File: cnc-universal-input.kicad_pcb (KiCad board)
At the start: 2 copper layers, 96.5 x 96.5 mm, 161 parts, among them J1 SA, J10 pwr-in, J11 output, J12 USB_B_Mini, J13 ext-pwr, J2 SB, J3 SC, J4 SD, J5 SE, J6 SF, J7 SG, J8 SH, J9 AVR-ISP-6, Q1 2N7002, Q10 IRLML2244TRPBF, Q11 2N7002, Q12 2N7002, Q13 2N7002, Q2 2N7002, Q3 2N7002, Q4 2N7002, Q5 2N7002, Q6 2N7002, Q7 2N7002, Q8 2N7002, Q9 2N7002, SW1 RESET, SW2 BTN, U1 ATmega328PB, U10 SFH617A-4, U11 SFH617A-4, U12 SFH617A-4, U13 SFH617A-4, U14 SFH617A-4, U15 SFH617A-4, U16 SFH617A-4, U17 SFH617A-4, U18 CH340G, U2 74HC595, U3 74HC595, U4 74HC595, U5 4051, U6 L7812, U7 L7805, U8 LM7321, U9 SFH617A-4, Y1 20Mhz, Y2 12MHz

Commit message: Fixed 340G isolation issue
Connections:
- C10 pad 1: VBUS -> +5V
- C21 pad 1: VBUS -> +5V
- J12 pad 1: VBUS -> (no net)
- J12 pad 4: Net-(J12-Pad4) -> (no net)
- R66 pad 1: VBUS -> +5V
- R67 pad 1: VBUS -> +5V
- U18 pad 10: Net-(U18-Pad10) -> (no net)
- U18 pad 11: Net-(U18-Pad11) -> (no net)
- U18 pad 12: Net-(U18-Pad12) -> (no net)
- U18 pad 13: Net-(U18-Pad13) -> (no net)
- U18 pad 14: Net-(U18-Pad14) -> (no net)
- U18 pad 15: Net-(U18-Pad15) -> (no net)
- U18 pad 16: VBUS -> +5V
- U18 pad 9: Net-(U18-Pad9) -> (no net)
- U2 pad 9: Net-(U2-Pad9) -> (no net)
- U3 pad 9: Net-(U3-Pad9) -> (no net)
- U4 pad 9: Net-(U4-Pad9) -> (no net)
- U8 pad 1: Net-(U8-Pad1) -> (no net)
- U8 pad 5: Net-(U8-Pad5) -> (no net)
- U8 pad 8: Net-(U8-Pad8) -> (no net)
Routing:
- net +5V: track 161.7 -> 235.6 mm, vias 4 -> 8
- net VBUS: track 51.0 -> 0.00 mm
- net GND: vias 234 -> 238

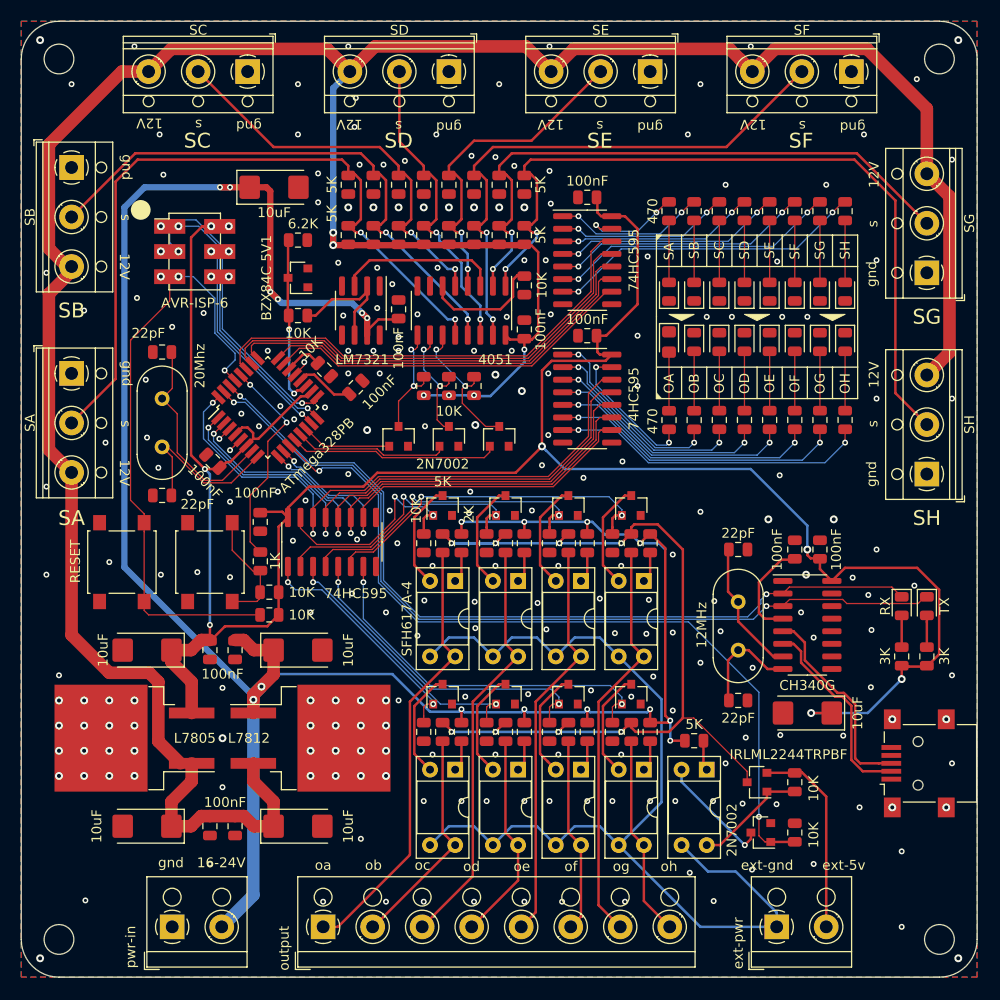
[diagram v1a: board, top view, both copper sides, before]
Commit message: Changed the voltage divider
Forgot to change R2 to 10K/7K so the input voltage to the adc was a bit low. 4.5 instead of 4.9.
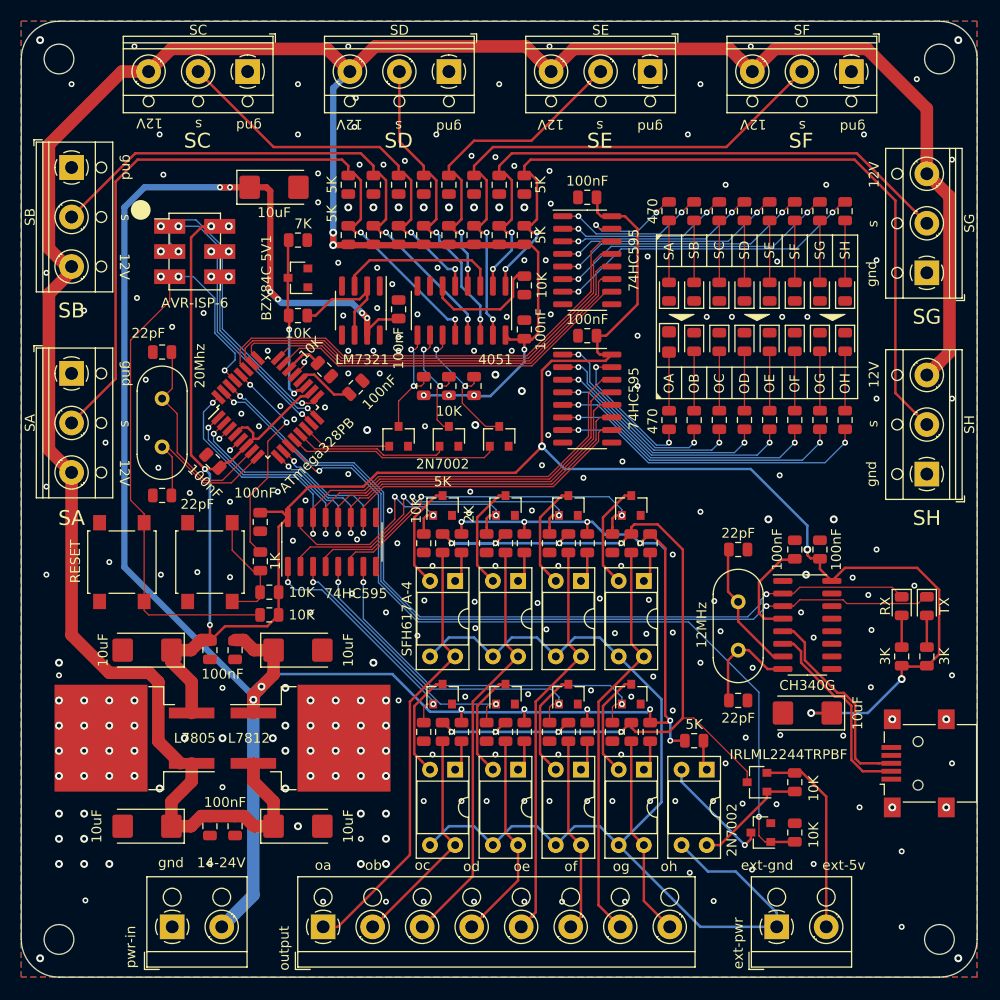
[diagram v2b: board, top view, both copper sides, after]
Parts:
- R35: value 6.2K -> 7K
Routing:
- net GND: vias 238 -> 260
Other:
- board text added: "14-24V"
- board text removed: "16-24V"
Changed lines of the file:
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@@
     (thickness 1.6)
     (drawings 85)
-    (tracks 1603)
+    (tracks 1625)
     (zones 0)
     (modules 161)
@@
       (effects (font (size 1 1) (thickness 0.15)))
     )
-    (fp_text value 6.2K (at 0.508 -1.651 180) (layer F.SilkS)
+    (fp_text value 7K (at 0.508 -1.651 180) (layer F.SilkS)
       (effects (font (size 1 1) (thickness 0.15)))
     )
@@
     (effects (font (size 1 1) (thickness 0.15)))
   )
-  (gr_text 16-24V (at 195.453 -24.257) (layer F.SilkS)
+  (gr_text 14-24V (at 195.453 -24.257) (layer F.SilkS)
     (effects (font (size 1 1) (thickness 0.15)))
   )
@@
   (via (at 250.698 -58.928) (size 0.8) (drill 0.4) (layers F.Cu B.Cu) (net 2))
   (via (at 195.58 -36.83) (size 0.8) (drill 0.4) (layers F.Cu B.Cu) (net 2))
+  (via (at 179.07 -29.21) (size 0.8) (drill 0.4) (layers F.Cu B.Cu) (net 2))
+  (via (at 179.07 -26.67) (size 0.8) (drill 0.4) (layers F.Cu B.Cu) (net 2))
+  (via (at 179.07 -24.13) (size 0.8) (drill 0.4) (layers F.Cu B.Cu) (net 2))
+  (via (at 181.61 -29.21) (size 0.8) (drill 0.4) (layers F.Cu B.Cu) (net 2))
+  (via (at 181.61 -26.67) (size 0.8) (drill 0.4) (layers F.Cu B.Cu) (net 2))
+  (via (at 181.61 -24.13) (size 0.8) (drill 0.4) (layers F.Cu B.Cu) (net 2))
+  (via (at 179.07 -44.45) (size 0.8) (drill 0.4) (layers F.Cu B.Cu) (net 2))
+  (via (at 212.09 -29.21) (size 0.8) (drill 0.4) (layers F.Cu B.Cu) (net 2))
+  (via (at 209.55 -29.21) (size 0.8) (drill 0.4) (layers F.Cu B.Cu) (net 2))
+  (via (at 212.09 -26.67) (size 0.8) (drill 0.4) (layers F.Cu B.Cu) (net 2))
+  (via (at 212.09 -24.13) (size 0.8) (drill 0.4) (layers F.Cu B.Cu) (net 2))
+  (via (at 209.55 -24.13) (size 0.8) (drill 0.4) (layers F.Cu B.Cu) (net 2))
+  (via (at 210.82 -44.45) (size 0.8) (drill 0.4) (layers F.Cu B.Cu) (net 2))
+  (via (at 200.66 -36.83) (size 0.8) (drill 0.4) (layers F.Cu B.Cu) (net 2))
+  (via (at 201.93 -41.91) (size 0.8) (drill 0.4) (layers F.Cu B.Cu) (net 2))
+  (via (at 201.93 -31.75) (size 0.8) (drill 0.4) (layers F.Cu B.Cu) (net 2))
+  (via (at 201.93 -35.56) (size 0.8) (drill 0.4) (layers F.Cu B.Cu) (net 2))
+  (via (at 201.93 -38.1) (size 0.8) (drill 0.4) (layers F.Cu B.Cu) (net 2))
+  (via (at 191.77 -36.83) (size 0.8) (drill 0.4) (layers F.Cu B.Cu) (net 2))
+  (via (at 189.23 -31.75) (size 0.8) (drill 0.4) (layers F.Cu B.Cu) (net 2))
+  (via (at 184.15 -24.13) (size 0.8) (drill 0.4) (layers F.Cu B.Cu) (net 2))
+  (via (at 203.2 -27.94) (size 0.8) (drill 0.4) (layers F.Cu B.Cu) (net 2))
   (segment (start 190.509 -65.215) (end 190.509 -61.341) (width 0.127) (layer F.Cu) (net 3))
   (segment (start 189.484 -66.24) (end 190.509 -65.215) (width 0.127) (layer F.Cu) (net 3))
@@
   (segment (start 254.635 -55.88) (end 254.635 -55.314315) (width 0.25) (layer F.Cu) (net 6))
   (segment (start 254.958315 -54.991) (end 255.52599 -54.991) (width 0.25) (layer F.Cu) (net 6))
+  (segment (start 264.86 -44.06) (end 266.7 -44.06) (width 0.254) (layer F.Cu) (net 6))
+  (segment (start 264.16 -44.06) (end 264.86 -44.06) (width 0.254) (layer F.Cu) (net 6))
+  (segment (start 255.905 -53.91) (end 257.11 -52.705) (width 0.254) (layer F.Cu) (net 6))
+  (segment (start 255.905 -54.855) (end 255.905 -53.91) (width 0.254) (layer F.Cu) (net 6))
+  (segment (start 267.94 -51.81) (end 267.94 -45.3) (width 0.254) (layer F.Cu) (net 6))
+  (segment (start 265.72 -54.03) (end 267.94 -51.81) (width 0.254) (layer F.Cu) (net 6))
+  (segment (start 267.94 -45.3) (end 266.7 -44.06) (width 0.254) (layer F.Cu) (net 6))
+  (segment (start 257.11 -52.705) (end 258.435 -54.03) (width 0.254) (layer F.Cu) (net 6))
+  (segment (start 258.435 -54.03) (end 265.72 -54.03) (width 0.254) (layer F.Cu) (net 6))
+  (via (at 255.016 -39.37) (size 0.8) (drill 0.4) (layers F.Cu B.Cu) (net 6))
+  (segment (start 257.0975 -39.37) (end 255.016 -39.37) (width 0.25) (layer F.Cu) (net 6))
+  (segment (start 255.016 -39.37) (end 255.581685 -39.37) (width 0.25) (layer B.Cu) (net 6))
+  (via (at 264.16 -42.799) (size 0.8) (drill 0.4) (layers F.Cu B.Cu) (net 6))
+  (segment (start 255.581685 -39.37) (end 260.731 -39.37) (width 0.25) (layer B.Cu) (net 6))
+  (segment (start 260.731 -39.37) (end 264.16 -42.799) (width 0.25) (layer B.Cu) (net 6))
+  (segment (start 264.16 -42.799) (end 264.16 -44.1475) (width 0.25) (layer F.Cu) (net 6))
   (segment (start 202.175 -83.287) (end 202.2 -83.312) (width 0.254) (layer F.Cu) (net 7))
   (segment (start 202.175 -79.502) (end 202.175 -83.287) (width 0.254) (layer F.Cu) (net 7))
@@
   (segment (start 203.440047 -72.953361) (end 204.019686 -73.533) (width 0.254) (layer F.Cu) (net 106))
   (segment (start 204.019686 -73.533) (end 204.851 -73.533) (width 0.254) (layer F.Cu) (net 106))
-  (segment (start 264.86 -44.06) (end 266.7 -44.06) (width 0.254) (layer F.Cu) (net 6))
-  (segment (start 264.16 -44.06) (end 264.86 -44.06) (width 0.254) (layer F.Cu) (net 6))
-  (segment (start 255.905 -53.91) (end 257.11 -52.705) (width 0.254) (layer F.Cu) (net 6))
-  (segment (start 255.905 -54.855) (end 255.905 -53.91) (width 0.254) (layer F.Cu) (net 6))
-  (segment (start 267.94 -51.81) (end 267.94 -45.3) (width 0.254) (layer F.Cu) (net 6))
-  (segment (start 265.72 -54.03) (end 267.94 -51.81) (width 0.254) (layer F.Cu) (net 6))
-  (segment (start 267.94 -45.3) (end 266.7 -44.06) (width 0.254) (layer F.Cu) (net 6))
-  (segment (start 257.11 -52.705) (end 258.435 -54.03) (width 0.254) (layer F.Cu) (net 6))
-  (segment (start 258.435 -54.03) (end 265.72 -54.03) (width 0.254) (layer F.Cu) (net 6))
-  (via (at 255.016 -39.37) (size 0.8) (drill 0.4) (layers F.Cu B.Cu) (net 6))
-  (segment (start 257.0975 -39.37) (end 255.016 -39.37) (width 0.25) (layer F.Cu) (net 6))
-  (segment (start 255.016 -39.37) (end 255.581685 -39.37) (width 0.25) (layer B.Cu) (net 6))
-  (via (at 264.16 -42.799) (size 0.8) (drill 0.4) (layers F.Cu B.Cu) (net 6))
-  (segment (start 255.581685 -39.37) (end 260.731 -39.37) (width 0.25) (layer B.Cu) (net 6))
-  (segment (start 260.731 -39.37) (end 264.16 -42.799) (width 0.25) (layer B.Cu) (net 6))
-  (segment (start 264.16 -42.799) (end 264.16 -44.1475) (width 0.25) (layer F.Cu) (net 6))
   (segment (start 246.625 -51.625) (end 247.65 -50.6) (width 0.254) (layer F.Cu) (net 107))
   (segment (start 246.625 -55.88) (end 246.625 -51.625) (width 0.254) (layer F.Cu) (net 107))
@@
   (segment (start 252.015 -54.855) (end 249.7455 -52.5855) (width 0.254) (layer F.Cu) (net 109))
   (segment (start 264.16 -49.14) (end 264.16 -46.11) (width 0.254) (layer F.Cu) (net 110))
-  (segment (start 252.46 -51.735) (end 252.16 -51.435) (width 0.127) (layer F.Cu) (net 111))
-  (segment (start 252.815 -52.09) (end 252.46 -51.735) (width 0.127) (layer F.Cu) (net 111))
-  (segment (start 263.17 -52.09) (end 252.815 -52.09) (width 0.127) (layer F.Cu) (net 111))
-  (segment (start 264.16 -51.19) (end 264.07 -51.19) (width 0.127) (layer F.Cu) (net 111))
-  (segment (start 264.07 -51.19) (end 263.17 -52.09) (width 0.127) (layer F.Cu) (net 111))
   (via (at 197.358 -71.374) (size 0.6) (drill 0.3) (layers F.Cu B.Cu) (net 111))
   (segment (start 196.344324 -72.387676) (end 197.358 -71.374) (width 0.127) (layer F.Cu) (net 111))
@@
   (segment (start 208.8515 -64.643) (end 211.836 -61.6585) (width 0.127) (layer B.Cu) (net 111))
   (segment (start 211.836 -61.6585) (end 211.836 -52.7685) (width 0.127) (layer B.Cu) (net 111))
+  (segment (start 253.873 -52.07) (end 253.238 -51.435) (width 0.127) (layer F.Cu) (net 111))
+  (segment (start 253.238 -51.435) (end 252.16 -51.435) (width 0.127) (layer F.Cu) (net 111))
+  (segment (start 263.19 -52.07) (end 253.873 -52.07) (width 0.127) (layer F.Cu) (net 111))
+  (segment (start 264.16 -51.19) (end 264.07 -51.19) (width 0.127) (layer F.Cu) (net 111))
+  (segment (start 264.07 -51.19) (end 263.19 -52.07) (width 0.127) (layer F.Cu) (net 111))
   (segment (start 266.7 -48.565) (end 266.7 -46.11) (width 0.254) (layer F.Cu) (net 112))
   (segment (start 266.7 -49.14) (end 266.7 -48.565) (width 0.254) (layer F.Cu) (net 112))
-  (segment (start 252.46 -50.465) (end 252.16 -50.165) (width 0.127) (layer F.Cu) (net 113))
-  (segment (start 252.835 -50.84) (end 252.46 -50.465) (width 0.127) (layer F.Cu) (net 113))
-  (segment (start 266.58 -51.19) (end 265.81449 -50.42449) (width 0.127) (layer F.Cu) (net 113))
-  (segment (start 266.7 -51.19) (end 266.58 -51.19) (width 0.127) (layer F.Cu) (net 113))
-  (segment (start 258.61551 -50.42449) (end 258.2 -50.84) (width 0.127) (layer F.Cu) (net 113))
-  (segment (start 265.81449 -50.42449) (end 258.61551 -50.42449) (width 0.127) (layer F.Cu) (net 113))
-  (segment (start 258.2 -50.84) (end 252.835 -50.84) (width 0.127) (layer F.Cu) (net 113))
   (via (at 196.723 -70.739) (size 0.6) (drill 0.3) (layers F.Cu B.Cu) (net 113))
   (segment (start 195.732583 -71.729417) (end 196.723 -70.739) (width 0.127) (layer F.Cu) (net 113))
@@
   (segment (start 215.413775 -48.8315) (end 211.581989 -52.663286) (width 0.127) (layer B.Cu) (net 113))
   (segment (start 211.581989 -61.531511) (end 208.7245 -64.389) (width 0.127) (layer B.Cu) (net 113))
+  (segment (start 253.238 -50.165) (end 252.16 -50.165) (width 0.127) (layer F.Cu) (net 113))
+  (segment (start 253.873 -50.8) (end 253.238 -50.165) (width 0.127) (layer F.Cu) (net 113))
+  (segment (start 266.58 -51.19) (end 265.81449 -50.42449) (width 0.127) (layer F.Cu) (net 113))
+  (segment (start 258.24 -50.8) (end 253.873 -50.8) (width 0.127) (layer F.Cu) (net 113))
+  (segment (start 265.81449 -50.42449) (end 258.61551 -50.42449) (width 0.127) (layer F.Cu) (net 113))
+  (segment (start 266.7 -51.19) (end 266.58 -51.19) (width 0.127) (layer F.Cu) (net 113))
+  (segment (start 258.61551 -50.42449) (end 258.24 -50.8) (width 0.127) (layer F.Cu) (net 113))
   (segment (start 263.211 -38.74) (end 263.211 -38.74) (width 0.127) (layer F.Cu) (net 114))
   (segment (start 268.661 -38.74) (end 268.661 -38.74) (width 0.127) (layer F.Cu) (net 114))

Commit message: Cleanup
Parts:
- removed Q10: IRLML2244TRPBF, Package_TO_SOT_SMD:SOT-23
- removed Q2, Q3, Q4, Q5, Q6, Q7, Q8, Q9: 2N7002, Package_TO_SOT_SMD:SOT-23
- removed R10, R11, R12, R13, R14, R15, R16, R2, R3, R4, R44, R45, R46, R47, R5, R56, R57, R58, R59, R6, R7, R8, R9: 5K, Resistor_SMD:R_0805_2012Metric
- removed R18, R19, R20, R21, R22, R23, R24, R25, R26, R27, R28, R29, R30, R31, R32, R33: 470, Resistor_SMD:R_0805_2012Metric
- removed R36, R37, R38, R39, R48, R49, R50, R51: 2K, Resistor_SMD:R_0805_2012Metric
- removed R40, R41, R42, R43, R52, R53, R54, R55, R61, R62, R63: 10K, Resistor_SMD:R_0805_2012Metric
- removed U17: SFH617A-4, Package_DIP:DIP-4_W7.62mm_Socket
- removed U7: L7805, Package_TO_SOT_SMD:TO-263-2
- added BZ1: Buzzer, Buzzer_Beeper:Buzzer_TDK_PS1240P02BT_D12.2mm_H6.5mm, F.Cu at (231.5, -57.4)
- added C24: 10nF, Capacitor_SMD:C_0805_2012Metric, F.Cu at (200.9, -46.5)
- added C25: 10uF, Capacitor_SMD:CP_Elec_4x5.4, F.Cu at (254.3, -36.8)
- added C26: 100nF, Capacitor_SMD:C_0805_2012Metric, F.Cu at (248.0, -36.2)
- added C27: 10uF, Capacitor_SMD:CP_Elec_4x5.4, F.Cu at (216.8, -89.4)
- added C28: 10uF, Capacitor_SMD:CP_Elec_4x5.4, F.Cu at (222.2, -53.5)
- added D20: B240F, Diode_SMD:D_2114_3652Metric, F.Cu at (207.8, -29.0)
- added D21: B240F, Diode_SMD:D_2114_3652Metric, F.Cu at (207.8, -41.7)
- added D22: LEDB, Diode_SMD:D_0805_2012Metric, F.Cu at (219.5, -57.4)
- added D23: BAT54A, Package_TO_SOT_SMD:SOT-23, F.Cu at (245.1, -32.3)
- added D24: BAT54A, Package_TO_SOT_SMD:SOT-23, F.Cu at (248.8, -32.3)
- added D25: BAT54A, Package_TO_SOT_SMD:SOT-23, F.Cu at (256.2, -32.3)
- added D26: BAT54A, Package_TO_SOT_SMD:SOT-23, F.Cu at (252.5, -32.3)
- added J14: 2PT, TerminalBlock_RND:TerminalBlock_RND_205-00001_1x02_P5.00mm_Horizontal, F.Cu at (200.2, -17.8)
- added L1: 68uH, Inductor_SMD:L_6.3x6.3_H3, F.Cu at (194.3, -29.2)
- added L2: 68uH, Inductor_SMD:L_6.3x6.3_H3, F.Cu at (194.3, -41.9)
- added R72: 4.7K, Resistor_SMD:R_0805_2012Metric, F.Cu at (188.2, -31.3)
- added R73: 1.5K, Resistor_SMD:R_0805_2012Metric, F.Cu at (188.2, -27.2)
- added R74: 9.1K, Resistor_SMD:R_0805_2012Metric, F.Cu at (188.3, -39.8)
- added R75: 1K, Resistor_SMD:R_0805_2012Metric, F.Cu at (188.3, -44.1)
- added RN1: 10KP4, Resistor_SMD:R_Array_Convex_4x1206, F.Cu at (247.0, -27.8)
- added RN10: 4.7KP4, Resistor_SMD:R_Array_Convex_4x1206, F.Cu at (222.1, -93.2)
- added RN11: 470P4, Resistor_SMD:R_Array_Convex_4x1206, F.Cu at (224.2, -48.3)
- added RN12: 470P4, Resistor_SMD:R_Array_Convex_4x1206, F.Cu at (230.5, -48.3)
- added RN2: 10KP4, Resistor_SMD:R_Array_Convex_4x1206, F.Cu at (254.4, -27.8)
- added RN3: 470P4, Resistor_SMD:R_Array_Convex_4x1206, F.Cu at (246.5, -90.2)
- added RN4: 470P4, Resistor_SMD:R_Array_Convex_4x1206, F.Cu at (252.5, -90.2)
- added RN5: 470P4, Resistor_SMD:R_Array_Convex_4x1206, F.Cu at (246.5, -68.6)
- added RN6: 470P4, Resistor_SMD:R_Array_Convex_4x1206, F.Cu at (252.5, -68.6)
- added RN7: 4.7KP4, Resistor_SMD:R_Array_Convex_4x1206, F.Cu at (211.3, -88.0)
- added RN8: 4.7KP4, Resistor_SMD:R_Array_Convex_4x1206, F.Cu at (211.3, -93.2)
- added RN9: 4.7KP4, Resistor_SMD:R_Array_Convex_4x1206, F.Cu at (222.1, -88.0)
- added U19: TS2596S, Package_SO:SOP-8_3.9x4.9mm_P1.27mm, F.Cu at (202.6, -28.7)
- C1, C11, C12, C2: value 22pF -> 30pF
- C10, C22: footprint Capacitor_Tantalum_SMD:CP_EIA-6032-28_Kemet-C -> Capacitor_SMD:CP_Elec_4x5.4
- C14, C8: value 10uF -> 100nF; footprint Capacitor_Tantalum_SMD:CP_EIA-6032-28_Kemet-C -> Capacitor_SMD:C_0805_2012Metric
- C15: value 100nF -> 10nF
- C3: value 10uF -> 150uF; footprint Capacitor_Tantalum_SMD:CP_EIA-6032-28_Kemet-C -> Capacitor_SMD:CP_Elec_6.3x7.7
- C5: value 100nF -> 10uF; footprint Capacitor_SMD:C_0805_2012Metric -> Capacitor_SMD:CP_Elec_4x5.4
- C6: value 100nF -> 220uF; footprint Capacitor_SMD:C_0805_2012Metric -> Capacitor_SMD:CP_Elec_6.3x7.7
- C7: value 10uF -> 220uF; footprint Capacitor_Tantalum_SMD:CP_EIA-6032-28_Kemet-C -> Capacitor_SMD:CP_Elec_6.3x7.7
- D1: value OA -> LEDO; footprint Diode_SMD:D_0805_2012Metric_Pad1.15x1.40mm_HandSolder -> LED_SMD:LED_0805_2012Metric
- D10: value SB -> LEDB
- D11: value SC -> LEDB
- D12: value SD -> LEDB
- D13: value SE -> LEDB
- D14: value SF -> LEDB
- D15: value SG -> LEDB
- D16: value SH -> LEDB
- D18: value RX -> LEDB
- D19: value TX -> LEDO
- D2: value OB -> LEDO
- D3: value OC -> LEDO
- D4: value OD -> LEDO
- D5: value OE -> LEDO
- D6: value OF -> LEDO
- D7: value OG -> LEDO
- D8: value OH -> LEDO
- D9: value SA -> LEDB
- J1: value SA -> 3PT
- J10: value pwr-in -> 2PT
- J11: value output -> 8PT
- J13: value ext-pwr -> 2PT
- J2: value SB -> 3PT
- J3: value SC -> 3PT
- J4: value SD -> 3PT
- J5: value SE -> 3PT
- J6: value SF -> 3PT
- J7: value SG -> 3PT
- J8: value SH -> 3PT
- R1: value 5K -> 330
- R35: value 7K -> 6.8K
- R60: value 5K -> 1K
- R66, R67: value 3K -> 2K
- U10, U11, U12, U13, U14, U15, U16, U9: footprint Package_DIP:DIP-4_W7.62mm_Socket -> Package_DIP:DIP-4_W7.62mm
- U6: value L7812 -> TS2596S; footprint Package_TO_SOT_SMD:TO-263-2 -> Package_SO:SOP-8_3.9x4.9mm_P1.27mm
- Y1: value 20Mhz -> 18.432Mhz
- moved C5 77.1 mm to (237.1, -93.7), turned to 0 degrees
- moved R60 34.0 mm to (219.5, -61.0), turned to 270 degrees
- moved R1 33.7 mm to (222.8, -57.1), turned to 0 degrees
- moved C7 26.4 mm to (181.6, -43.2), turned to 180 degrees
- moved C3 23.9 mm to (181.6, -35.6), turned to 180 degrees
- moved C6 21.8 mm to (181.6, -27.9), turned to 180 degrees
- moved C10 18.2 mm to (262.4, -55.9), turned to 0 degrees
- moved C8 12.9 mm to (194.3, -34.5), turned to 0 degrees
- moved C4 12.7 mm to (189.2, -35.6), turned to 0 degrees
- moved C14 10.7 mm to (194.3, -36.6), turned to 0 degrees
- moved C15 8.82 mm to (200.9, -33.8), turned to 0 degrees
- moved U11 8.25 mm to (225.4, -44.5)
- moved U13 8.25 mm to (231.8, -44.5)
- moved U15 8.25 mm to (238.1, -44.5)
- moved U9 8.25 mm to (219.1, -44.5)
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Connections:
- net /IN-SER renamed /DISP-SER
- net /OA renamed /BA
- net /OB renamed /BB
- net /OC renamed /BC
- net /OD renamed /BD
- net /OE renamed /BE
- net /OF renamed /BF
- net /OG renamed /BG
- net /OH renamed /BH
- C15 pad 1: +12V -> +5V
- C15 pad 2: GND -> Net-(C15-Pad2)
- C5 pad 1: +12V -> +5V
- Q1 pad 1: /OUT-A -> /TO
- Q1 pad 3: Net-(Q1-Pad3) -> Net-(BZ1-Pad2)
- R1 pad 2: /SA -> Net-(BZ1-Pad1)
- R60 pad 1: +24V -> Net-(R60-Pad1)
- U1 pad 1: /~OUT-OE -> /OUT-RCLK
- U1 pad 10: /~OUT-SRCLR -> /TO
- U1 pad 11: /EN-PULLUP -> Net-(R60-Pad1)
- U1 pad 2: /OUT-RCLK -> /OUT-SRCLK
- U1 pad 22: Net-(R63-Pad2) -> /ASIN
- U1 pad 23: /~IN-SRCLR -> /~DISP-SRCLR
- U1 pad 24: /IN-SRCLK -> /DISP-SRCLK
- U1 pad 25: /IN-RCLK -> /DISP-RCLK
- U1 pad 26: /~IN-OE -> /~DISP-OE
- U1 pad 9: /OUT-SRCLK -> /~OUT-SRCLR
- U10 pad 1: Net-(R37-Pad2) -> /POB
- U10 pad 2: Net-(Q2-Pad3) -> GND
- U11 pad 1: Net-(R38-Pad2) -> /POC
- U11 pad 2: Net-(Q3-Pad3) -> GND
- U12 pad 1: Net-(R39-Pad2) -> /POD
- U12 pad 2: Net-(Q4-Pad3) -> GND
- U13 pad 1: Net-(R48-Pad2) -> /POE
- U13 pad 2: Net-(Q5-Pad3) -> GND
- U14 pad 1: Net-(R49-Pad2) -> /POF
- U14 pad 2: Net-(Q6-Pad3) -> GND
- U15 pad 1: Net-(R50-Pad2) -> /POG
- U15 pad 2: Net-(Q7-Pad3) -> GND
- U16 pad 1: Net-(R51-Pad2) -> /POH
- U16 pad 2: Net-(Q8-Pad3) -> GND
- U2 pad 10: /~OUT-SRCLR -> /~DISP-SRCLR
- U2 pad 11: /OUT-SRCLK -> /DISP-SRCLK
- U2 pad 12: /OUT-RCLK -> /DISP-RCLK
- U2 pad 13: /~OUT-OE -> /~DISP-OE
- U2 pad 14: /OUT-SER -> /DISP-SER2
- U3 pad 13: /~OUT-OE -> GND
- U4 pad 10: /~IN-SRCLR -> /~DISP-SRCLR
- U4 pad 11: /IN-SRCLK -> /DISP-SRCLK
- U4 pad 12: /IN-RCLK -> /DISP-RCLK
- U4 pad 13: /~IN-OE -> /~DISP-OE
- U4 pad 9: (no net) -> /DISP-SER2
- U6 pad 2: GND -> Net-(D21-Pad1)
- U6 pad 3: +12V -> Net-(C24-Pad2)
- U9 pad 1: Net-(R36-Pad2) -> /POA
- U9 pad 2: Net-(Q1-Pad3) -> GND
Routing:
- net /BIAS: track 90.1 -> 0.00 mm, vias 8 -> 0
- net /EN-PULLUP: track 81.6 -> 0.00 mm, vias 2 -> 0
- net +24V: track 236.8 -> 170.1 mm, vias 18 -> 13
- net /~DISP-OE: track 0.00 -> 60.1 mm
- net /DISP-RCLK: track 0.00 -> 59.9 mm
- net /~OUT-OE: track 58.8 -> 0.00 mm, vias 2 -> 0
- net /~DISP-SRCLR: track 0.00 -> 58.3 mm
- net /DISP-SRCLK: track 0.00 -> 57.3 mm
- net +5V: track 235.6 -> 284.0 mm, vias 8 -> 12
- net /~IN-OE: track 46.2 -> 0.00 mm
- net +12V: track 294.4 -> 339.5 mm, vias 6 -> 11
- net /IN-RCLK: track 44.0 -> 0.00 mm
- net /OUT-SER: track 62.9 -> 20.8 mm
- net /IN-SRCLK: track 39.3 -> 0.00 mm
- net /OUT-RCLK: track 57.7 -> 20.0 mm
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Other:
- outline, holes or cut-outs redrawn
- board text added: "+12V"
- board text added: "+5V"
- board text added: "16-30V"
- board text added: "3.4mm"
- board text added: "88.9"
- board text added: "BAUD 115200"
- board text added: "CONFIG"
- board text added: "OA"
- board text added: "OB"
- board text added: "OC"
- board text added: "OD"
- board text added: "OE"
- board text added: "OF"
- board text added: "OG"
- board text added: "OH"
- board text added: "RX"
- board text added: "TX"
- board text added: "UCNC"
- board text added: "ext-pwr"
- board text added: "ext-vin"
- board text added: "output"
- board text added: "pwr-in"
- board text added: "pwr-out"
- board text added: "v1.3"
- board text removed: "14-24V"
- board text removed: "ext-5v"
- board text removed: "v1.0"
